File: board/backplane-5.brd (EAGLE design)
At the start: 100 x 100 mm, 143 parts, among them CN1 RJ45JACK90, U1 AMS1117-5.0, U10 RT9193, U11 KSZ9897, U12 KSZ8081MLX, U13 STM32F217-100, U2 AMS1117-5.0, U3 AMS1117-5.0, U4 AMS1117-5.0, U5 AMS1117-5.0, U6 AMS1117-2.5, U7 AMS1117-1.2, U8 RT9193, U9 AMS1117-5.0, X1 25MHz, X2 25MHz

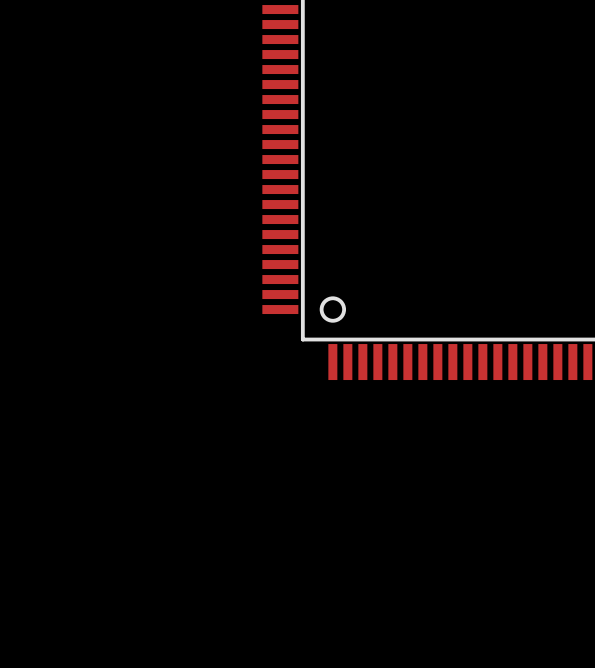
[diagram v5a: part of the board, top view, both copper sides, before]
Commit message: Added STM Crystal and fixed some devices
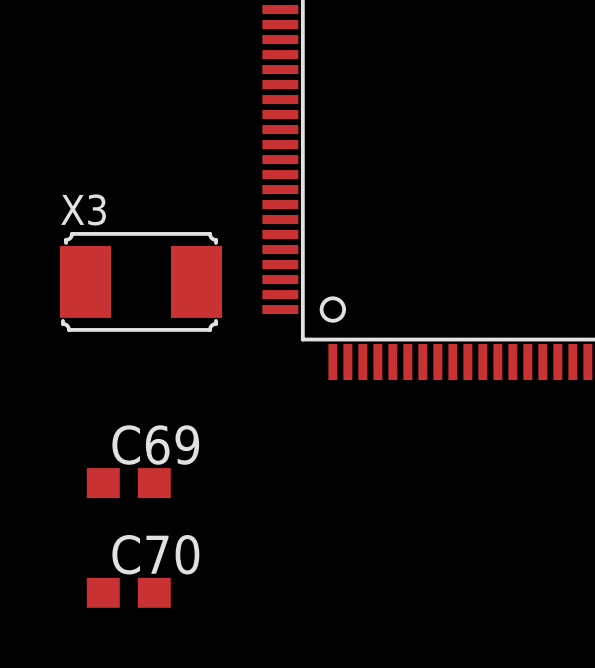
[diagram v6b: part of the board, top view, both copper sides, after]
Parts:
- added C69, C70: 8pF, tuetuopay:0603
- added X3: 25MHz, tuetuopay:XTAL-2-SMD
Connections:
- new net N$21: C69.1, U13.13, X3.P$1
- new net N$22: C70.1, U13.12, X3.P$2
- net GND: now also C69.2, C70.2
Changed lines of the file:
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@@
 </element>
 <element name="U13" library="tuetuopay" package="LQFP-100" value="STM32F217-100" x="-138.3792" y="-526.288"/>
+<element name="X3" library="tuetuopay" package="XTAL-2-SMD" value="25MHz" x="-150.7744" y="-531.368"/>
+<element name="C69" library="tuetuopay" package="0603" value="8pF" x="-151.1808" y="-538.0736"/>
+<element name="C70" library="tuetuopay" package="0603" value="8pF" x="-151.1808" y="-541.7312"/>
 </elements>
 <signals>
@@
 <contactref element="CN1" pad="S@1"/>
 <contactref element="CN1" pad="S@2"/>
+<contactref element="C70" pad="2"/>
+<contactref element="C69" pad="2"/>
 <wire x1="-106.26" y1="-387.35" x2="-106.26" y2="-400.05" width="0" layer="19" extent="1-1"/>
 <wire x1="-106.26" y1="-374.65" x2="-106.26" y2="-387.35" width="0" layer="19" extent="1-1"/>
@@
 <wire x1="-145.2" y1="-483.87" x2="-145.2" y2="-478.79" width="0" layer="19" extent="1-1"/>
 <wire x1="-134.62" y1="-509.27" x2="-145.2" y2="-483.87" width="0" layer="19" extent="1-1"/>
+<wire x1="-150.3308" y1="-538.0736" x2="-134.62" y2="-509.27" width="0" layer="19" extent="1-1"/>
+<wire x1="-150.3308" y1="-541.7312" x2="-150.3308" y2="-538.0736" width="0" layer="19" extent="1-1"/>
 <wire x1="-76.62" y1="-128.27" x2="-84.24" y2="-219.71" width="0" layer="19" extent="1-1"/>
 <wire x1="12.44" y1="5.83" x2="-76.62" y2="-128.27" width="0" layer="19" extent="1-1"/>
@@
 <wire x1="77.5" y1="3.5" x2="72.8" y2="8.05" width="0" layer="19" extent="1-1"/>
 <wire x1="90.4494" y1="36.1442" x2="76.4404" y2="35.3568" width="0" layer="19" extent="1-1"/>
-<wire x1="90.4494" y1="19.939" x2="90.4494" y2="36.1442" width="0" layer="19" extent="1-1"/>
-<wire x1="91.7984" y1="8.3312" x2="90.4494" y2="19.939" width="0" layer="19" extent="1-1"/>
+<wire x1="91.7984" y1="8.3312" x2="77.5" y2="3.5" width="0" layer="19" extent="1-1"/>
+<wire x1="90.4494" y1="19.939" x2="91.7984" y2="8.3312" width="0" layer="19" extent="1-1"/>
 <wire x1="76.5" y1="63" x2="76.4404" y2="39.0144" width="0" layer="19" extent="1-1"/>
 <wire x1="70.95" y1="73.3" x2="76.5" y2="63" width="0" layer="19" extent="1-1"/>
@@
 <wire x1="82.42555" y1="27.051" x2="89.027" y2="27.051" width="0.2032" layer="16"/>
 </signal>
+<signal name="N$21">
+<contactref element="X3" pad="P$1"/>
+<contactref element="U13" pad="13"/>
+<contactref element="C69" pad="1"/>
+<wire x1="-152.6244" y1="-531.368" x2="-152.0308" y2="-538.0736" width="0" layer="19" extent="1-1"/>
+<wire x1="-138.3792" y1="-534.038" x2="-152.0308" y2="-538.0736" width="0" layer="19" extent="1-1"/>
+</signal>
+<signal name="N$22">
+<contactref element="C70" pad="1"/>
+<contactref element="U13" pad="12"/>
+<contactref element="X3" pad="P$2"/>
+<wire x1="-148.9244" y1="-531.368" x2="-152.0308" y2="-541.7312" width="0" layer="19" extent="1-1"/>
+<wire x1="-138.8792" y1="-534.038" x2="-148.9244" y2="-531.368" width="0" layer="19" extent="1-1"/>
+</signal>
 </signals>

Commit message: Fixed the naming of some components (incl. library)
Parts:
- renumbered U$1 to CN2, U$2 to CN3, U$3 to CN4, U$4 to CN5, U$5 to CN6, X1 to Y1, X2 to Y2, X3 to Y3
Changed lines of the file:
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@@
 <element name="U9" library="tuetuopay" package="SOT223" value="AMS1117-5.0" x="18.89" y="6.45"/>
 <element name="RJ1" library="tuetuopay" package="RJ45MALE" value="RJ45PLUG" x="88" y="50" rot="R270"/>
-<element name="U$1" library="tuetuopay" package="4PINCONN-FEMALE-1.6" value="4PINCONNFEMALE-1.6" x="90" y="87" rot="R90"/>
+<element name="CN2" library="tuetuopay" package="4PINCONN-FEMALE-1.6" value="4PINCONNFEMALE-1.6" x="90" y="87" rot="R90"/>
 <element name="RJ2" library="tuetuopay" package="RJ45MALE" value="RJ45PLUG" x="68" y="50" rot="R270"/>
-<element name="U$2" library="tuetuopay" package="4PINCONN-FEMALE-1.6" value="4PINCONNFEMALE-1.6" x="70" y="87" rot="R90"/>
+<element name="CN3" library="tuetuopay" package="4PINCONN-FEMALE-1.6" value="4PINCONNFEMALE-1.6" x="70" y="87" rot="R90"/>
 <element name="RJ3" library="tuetuopay" package="RJ45MALE" value="RJ45PLUG" x="48" y="50" rot="R270"/>
-<element name="U$3" library="tuetuopay" package="4PINCONN-FEMALE-1.6" value="4PINCONNFEMALE-1.6" x="50" y="87" rot="R90"/>
+<element name="CN4" library="tuetuopay" package="4PINCONN-FEMALE-1.6" value="4PINCONNFEMALE-1.6" x="50" y="87" rot="R90"/>
 <element name="RJ4" library="tuetuopay" package="RJ45MALE" value="RJ45PLUG" x="28" y="50" rot="R270"/>
-<element name="U$4" library="tuetuopay" package="4PINCONN-FEMALE-1.6" value="4PINCONNFEMALE-1.6" x="30" y="87" rot="R90"/>
+<element name="CN5" library="tuetuopay" package="4PINCONN-FEMALE-1.6" value="4PINCONNFEMALE-1.6" x="30" y="87" rot="R90"/>
 <element name="RJ5" library="tuetuopay" package="RJ45MALE" value="RJ45PLUG" x="8" y="50" rot="R270"/>
-<element name="U$5" library="tuetuopay" package="4PINCONN-FEMALE-1.6" value="4PINCONNFEMALE-1.6" x="10" y="87" rot="R90"/>
+<element name="CN6" library="tuetuopay" package="4PINCONN-FEMALE-1.6" value="4PINCONNFEMALE-1.6" x="10" y="87" rot="R90"/>
 <element name="U11" library="tuetuopay" package="TQFP-128" value="KSZ9897" x="58.928" y="29.2608" rot="R270"/>
 <element name="C23" library="tuetuopay" package="0603" value="220uF" x="45.3644" y="31.9532" smashed="yes" rot="R180">
@@
 <attribute name="NAME" x="-79.375" y="-121.285" size="0.762" layer="25"/>
 </element>
-<element name="X1" library="tuetuopay" package="XTAL-2-SMD" value="25MHz" x="72.136" y="37.1856" smashed="yes" rot="R90">
+<element name="Y1" library="tuetuopay" package="XTAL-2-SMD" value="25MHz" x="72.136" y="37.1856" smashed="yes" rot="R90">
 <attribute name="NAME" x="70.236" y="34.4856" size="0.762" layer="21" font="vector" rot="R90"/>
 </element>
@@
 <attribute name="NAME" x="20.955" y="29.0322" size="0.762" layer="25" rot="R180"/>
 </element>
-<element name="X2" library="tuetuopay" package="XTAL-2-SMD" value="25MHz" x="26.0096" y="19.1008" smashed="yes" rot="R180">
+<element name="Y2" library="tuetuopay" package="XTAL-2-SMD" value="25MHz" x="26.0096" y="19.1008" smashed="yes" rot="R180">
 <attribute name="NAME" x="28.7096" y="17.2008" size="0.762" layer="21" font="vector" rot="R180"/>
 </element>
@@
 </element>
 <element name="U13" library="tuetuopay" package="LQFP-100" value="STM32F217-100" x="-138.3792" y="-526.288"/>
-<element name="X3" library="tuetuopay" package="XTAL-2-SMD" value="25MHz" x="-150.7744" y="-531.368"/>
+<element name="Y3" library="tuetuopay" package="XTAL-2-SMD" value="25MHz" x="-150.7744" y="-531.368"/>
 <element name="C69" library="tuetuopay" package="0603" value="8pF" x="-151.1808" y="-538.0736"/>
 <element name="C70" library="tuetuopay" package="0603" value="8pF" x="-151.1808" y="-541.7312"/>
@@
 <contactref element="C21" pad="2"/>
 <contactref element="C20" pad="2"/>
-<contactref element="U$1" pad="4@2"/>
-<contactref element="U$1" pad="4@1"/>
-<contactref element="U$2" pad="4@2"/>
-<contactref element="U$2" pad="4@1"/>
-<contactref element="U$3" pad="4@2"/>
-<contactref element="U$3" pad="4@1"/>
-<contactref element="U$4" pad="4@2"/>
-<contactref element="U$4" pad="4@1"/>
-<contactref element="U$5" pad="4@2"/>
-<contactref element="U$5" pad="4@1"/>
+<contactref element="CN2" pad="4@2"/>
+<contactref element="CN2" pad="4@1"/>
+<contactref element="CN3" pad="4@2"/>
+<contactref element="CN3" pad="4@1"/>
+<contactref element="CN4" pad="4@2"/>
+<contactref element="CN4" pad="4@1"/>
+<contactref element="CN5" pad="4@2"/>
+<contactref element="CN5" pad="4@1"/>
+<contactref element="CN6" pad="4@2"/>
+<contactref element="CN6" pad="4@1"/>
 <contactref element="U11" pad="P$138"/>
 <contactref element="U11" pad="P$150"/>
@@
 <contactref element="U5" pad="2"/>
 <contactref element="C9" pad="P"/>
-<contactref element="U$5" pad="1@2"/>
-<contactref element="U$5" pad="1@1"/>
+<contactref element="CN6" pad="1@2"/>
+<contactref element="CN6" pad="1@1"/>
 <wire x1="7.675" y1="75.557871875" x2="7.675" y2="71.065259375" width="0.8128" layer="1"/>
 <wire x1="7.675" y1="75.557871875" x2="7.675" y2="81" width="0.8128" layer="1"/>
@@
 <contactref element="U1" pad="2"/>
 <contactref element="C2" pad="P"/>
-<contactref element="U$1" pad="1@2"/>
-<contactref element="U$1" pad="1@1"/>
+<contactref element="CN2" pad="1@2"/>
+<contactref element="CN2" pad="1@1"/>
 <wire x1="87.675" y1="75.76655" x2="87.675" y2="81" width="0.8128" layer="1"/>
 <wire x1="87.675" y1="75.76655" x2="87.675" y2="71" width="0.8128" layer="1"/>
@@
 <contactref element="U2" pad="2"/>
 <contactref element="C3" pad="P"/>
-<contactref element="U$2" pad="1@2"/>
-<contactref element="U$2" pad="1@1"/>
+<contactref element="CN3" pad="1@2"/>
+<contactref element="CN3" pad="1@1"/>
 <wire x1="67.675" y1="75.574596875" x2="67.675" y2="81" width="0.8128" layer="1"/>
 <wire x1="67.675" y1="75.574596875" x2="67.675" y2="71" width="0.8128" layer="1"/>
@@
 <contactref element="U3" pad="2"/>
 <contactref element="C5" pad="P"/>
-<contactref element="U$3" pad="1@2"/>
-<contactref element="U$3" pad="1@1"/>
+<contactref element="CN4" pad="1@2"/>
+<contactref element="CN4" pad="1@1"/>
 <wire x1="47.675" y1="75.71170625" x2="47.675" y2="81" width="0.8128" layer="1"/>
 <wire x1="47.675" y1="75.71170625" x2="47.675" y2="71" width="0.8128" layer="1"/>
@@
 <contactref element="U4" pad="2"/>
 <contactref element="C7" pad="P"/>
-<contactref element="U$4" pad="1@2"/>
-<contactref element="U$4" pad="1@1"/>
+<contactref element="CN5" pad="1@2"/>
+<contactref element="CN5" pad="1@1"/>
 <wire x1="27.675" y1="75.729246875" x2="27.675" y2="81" width="0.8128" layer="1"/>
 <wire x1="27.675" y1="75.729246875" x2="27.675" y2="71" width="0.8128" layer="1"/>
@@
 </signal>
 <signal name="N$5">
-<contactref element="X1" pad="P$2"/>
+<contactref element="Y1" pad="P$2"/>
 <contactref element="C25" pad="1"/>
 <contactref element="U11" pad="P$126"/>
@@
 <signal name="N$6">
 <contactref element="C26" pad="1"/>
-<contactref element="X1" pad="P$1"/>
+<contactref element="Y1" pad="P$1"/>
 <contactref element="U11" pad="P$125"/>
 <wire x1="66.528" y1="34.2608" x2="67.91073125" y2="34.2608" width="0.2032" layer="1"/>
@@
 <signal name="N$9">
 <contactref element="U12" pad="15"/>
-<contactref element="X2" pad="P$1"/>
+<contactref element="Y2" pad="P$1"/>
 <contactref element="C66" pad="1"/>
 <wire x1="27.6352" y1="16.2932" x2="27.6352" y2="18.8764" width="0.2032" layer="1"/>
@@
 </signal>
 <signal name="N$10">
-<contactref element="X2" pad="P$2"/>
+<contactref element="Y2" pad="P$2"/>
 <contactref element="U12" pad="14"/>
 <contactref element="C67" pad="1"/>
@@
 </signal>
 <signal name="N$21">
-<contactref element="X3" pad="P$1"/>
+<contactref element="Y3" pad="P$1"/>
 <contactref element="U13" pad="13"/>
 <contactref element="C69" pad="1"/>
@@
 <contactref element="C70" pad="1"/>
 <contactref element="U13" pad="12"/>
-<contactref element="X3" pad="P$2"/>
+<contactref element="Y3" pad="P$2"/>
 <wire x1="-148.9244" y1="-531.368" x2="-152.0308" y2="-541.7312" width="0" layer="19" extent="1-1"/>
 <wire x1="-138.8792" y1="-534.038" x2="-148.9244" y2="-531.368" width="0" layer="19" extent="1-1"/>
